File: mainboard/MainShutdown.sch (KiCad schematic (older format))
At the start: 21 parts, among them J10 AIR+, J6 AIR-, K1 KT12-1A, K2 G6DN 12V, Q1 NTR4003N, U13 TS3704IPT, U14 CD4044, U15 CD4082, U4 MainBoard_AD8244

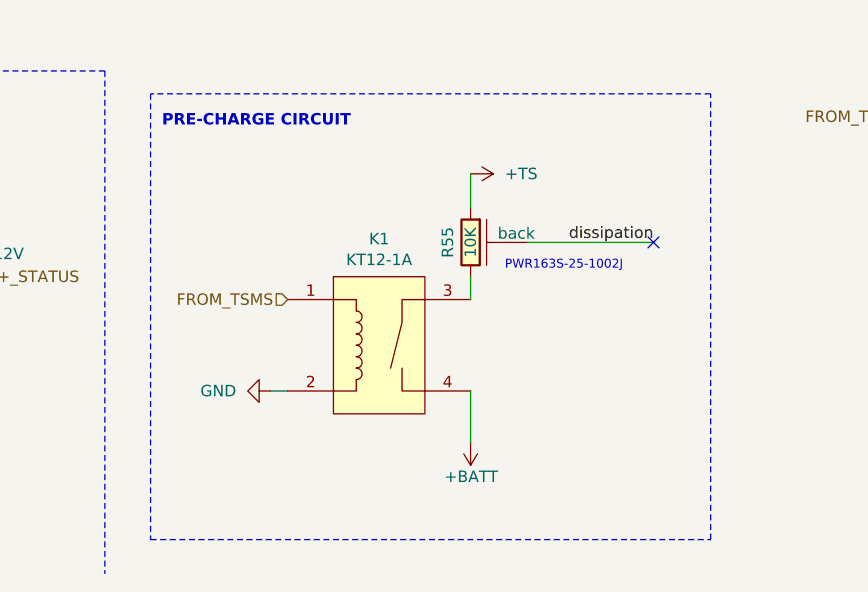
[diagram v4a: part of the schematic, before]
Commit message: added precharge rele suppression diode
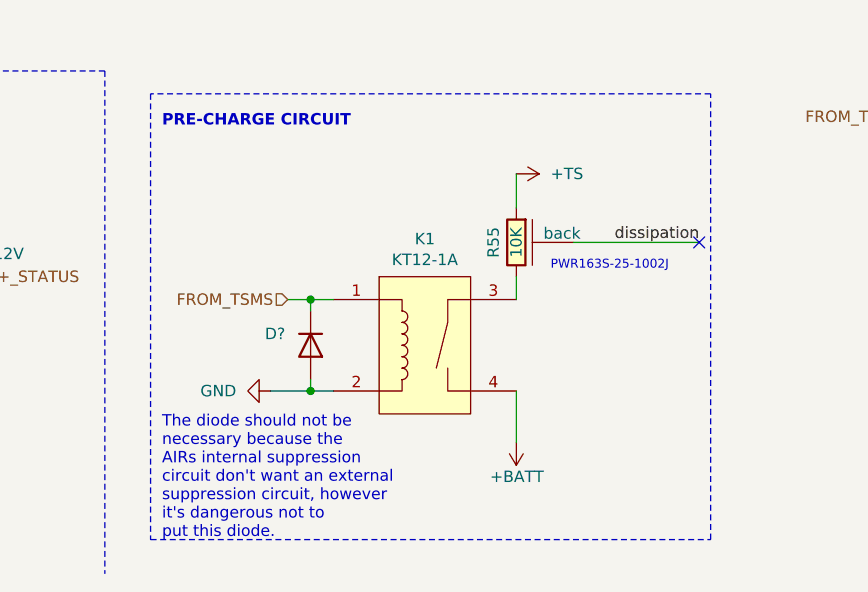
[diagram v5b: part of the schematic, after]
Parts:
- added D?: D, MainBoard:SOD_323HE, symbol Device:D
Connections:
- net FROM_TSMS: now also D?.1 (K)
- net GND: now also D?.2 (A)
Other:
- note added: "The diode should not be \nnecessary because the \nAIRs internal suppression \ncircuit don't want an external \nsuppression circuit, however \nit's dangerous not to \nput this diode."
- moved on the sheet: K1, R55
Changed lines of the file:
@@
 Comment4 ""
 $EndDescr
-Text Notes 6000 6375 0    39   ~ 0
+Text Notes 6200 6375 0    39   ~ 0
 PWR163S-25-1002J
 $Comp
 L MainBoard:+TS #PWR0148
 U 1 1 5B0DE0E2
-P 5850 5950
-F 0 "#PWR0148" H 5850 5800 50  0001 C CNN
-F 1 "+TS" V 5850 6100 50  0000 L CNN
-F 2 "" H 5750 5700 50  0001 C CNN
-F 3 "" H 5850 5800 50  0001 C CNN
-	1    5850 5950
+P 6050 5950
+F 0 "#PWR0148" H 6050 5800 50  0001 C CNN
+F 1 "+TS" V 6050 6100 50  0000 L CNN
+F 2 "" H 5950 5700 50  0001 C CNN
+F 3 "" H 6050 5800 50  0001 C CNN
+	1    6050 5950
 	0    1    1    0
 $EndComp
@@
 L power:+BATT #PWR0147
 U 1 1 5C2C487D
-P 5850 7125
-F 0 "#PWR0147" H 5850 6975 50  0001 C CNN
-F 1 "+BATT" H 5730 7275 50  0000 L CNN
-F 2 "" H 5850 7125 50  0001 C CNN
-F 3 "" H 5850 7125 50  0001 C CNN
-	1    5850 7125
+P 6050 7125
+F 0 "#PWR0147" H 6050 6975 50  0001 C CNN
+F 1 "+BATT" H 5930 7275 50  0000 L CNN
+F 2 "" H 6050 7125 50  0001 C CNN
+F 3 "" H 6050 7125 50  0001 C CNN
+	1    6050 7125
 	-1   0    0    1
 $EndComp
 Wire Wire Line
-	5850 6400 5850 6500
-Wire Wire Line
-	5850 6100 5850 5950
-Wire Wire Line
-	5850 6900 5850 7125
+	6050 6400 6050 6500
+Wire Wire Line
+	6050 6100 6050 5950
+Wire Wire Line
+	6050 6900 6050 7125
 $Comp
 L MainBoard:KT12-1A K1
 U 1 1 5E5A93F5
-P 5450 6700
-F 0 "K1" H 5450 7165 50  0000 C CNN
-F 1 "KT12-1A" H 5450 7074 50  0000 C CNN
-F 2 "MainBoard:KT_THT" H 5450 6350 50  0001 C CNN
-F 3 "https://standexelectronics.com/viewer/pdfjs/web/viewer.php?file=https%3A%2F%2Fstandexelectronics.com%2Fwp-content%2Fuploads%2F2015%2F03%2FKT_V03.pdf" H 5450 6700 50  0001 C CNN
-	1    5450 6700
+P 5650 6700
+F 0 "K1" H 5650 7165 50  0000 C CNN
+F 1 "KT12-1A" H 5650 7074 50  0000 C CNN
+F 2 "MainBoard:KT_THT" H 5650 6350 50  0001 C CNN
+F 3 "https://standexelectronics.com/viewer/pdfjs/web/viewer.php?file=https%3A%2F%2Fstandexelectronics.com%2Fwp-content%2Fuploads%2F2015%2F03%2FKT_V03.pdf" H 5650 6700 50  0001 C CNN
+	1    5650 6700
 	1    0    0    -1
 $EndComp
@@
 L MainBoard:R_power_backplane R55
 U 1 1 5DC7CE9F
-P 5850 6250
-F 0 "R55" V 5950 6250 50  0000 C CNN
-F 1 "10K" V 5850 6250 50  0000 C CNN
-F 2 "MainBoard:pwr163" V 5810 6250 50  0001 C CNN
-F 3 "~" H 5850 6250 50  0001 C CNN
-F 4 "https://www.mouser.it/ProductDetail/Bourns/PWR163S-25-1002J?qs=%2Fha2pyFadugfff1oC4vY%252Bes8I7FN4jgvWF%2FMj%252B7BM%2FJuTCfu5H9AeA%3D%3D" H 5850 6250 50  0001 C CNN "Mouser"
-	1    5850 6250
+P 6050 6250
+F 0 "R55" V 6150 6250 50  0000 C CNN
+F 1 "10K" V 6050 6250 50  0000 C CNN
+F 2 "MainBoard:pwr163" V 6010 6250 50  0001 C CNN
+F 3 "~" H 6050 6250 50  0001 C CNN
+F 4 "https://www.mouser.it/ProductDetail/Bourns/PWR163S-25-1002J?qs=%2Fha2pyFadugfff1oC4vY%252Bes8I7FN4jgvWF%2FMj%252B7BM%2FJuTCfu5H9AeA%3D%3D" H 6050 6250 50  0001 C CNN "Mouser"
+	1    6050 6250
 	-1   0    0    1
 $EndComp
@@
 Text HLabel 1600 6300 2    50   Input ~ 0
 AIR-_STATUS
-Text Label 6650 6250 2    50   ~ 0
+Text Label 6850 6250 2    50   ~ 0
 dissipation
 Wire Wire Line
-	6100 6250 6650 6250
-NoConn ~ 6650 6250
+	6300 6250 6850 6250
+NoConn ~ 6850 6250
 Text HLabel 2800 3050 0    50   Input ~ 0
 RESET_BUTTON
@@
 Text HLabel 5050 6500 0    50   Input ~ 0
 FROM_TSMS
-Wire Wire Line
-	4975 6900 5050 6900
 $Comp
 L power:GND #PWR0145
@@
 Wire Wire Line
 	3050 6300 3000 6300
+$Comp
+L Device:D D?
+U 1 1 60603EB1
+P 5150 6700
+AR Path="/60603EB1" Ref="D?"  Part="1"
+AR Path="/5B045B0D/60603EB1" Ref="D?"  Part="1"
+F 0 "D?" V 5100 6500 50  0000 L CNN
+F 1 "D" V 5200 6500 50  0001 L CNN
+F 2 "MainBoard:SOD_323HE" H 5150 6700 50  0001 C CNN
+F 3 "~" H 5150 6700 50  0001 C CNN
+	1    5150 6700
+	0    1    1    0
+$EndComp
+Wire Wire Line
+	4975 6900 5150 6900
+Wire Wire Line
+	5150 6850 5150 6900
+Connection ~ 5150 6900
+Wire Wire Line
+	5150 6900 5250 6900
+Wire Wire Line
+	5050 6500 5150 6500
+Wire Wire Line
+	5150 6500 5150 6550
+Wire Wire Line
+	5250 6500 5150 6500
+Connection ~ 5150 6500
+Text Notes 4500 7550 0    50   ~ 0
+The diode should not be \nnecessary because the \nAIRs internal suppression \ncircuit don't want an external \nsuppression circuit, however \nit's dangerous not to \nput this diode.
 $EndSCHEMATC

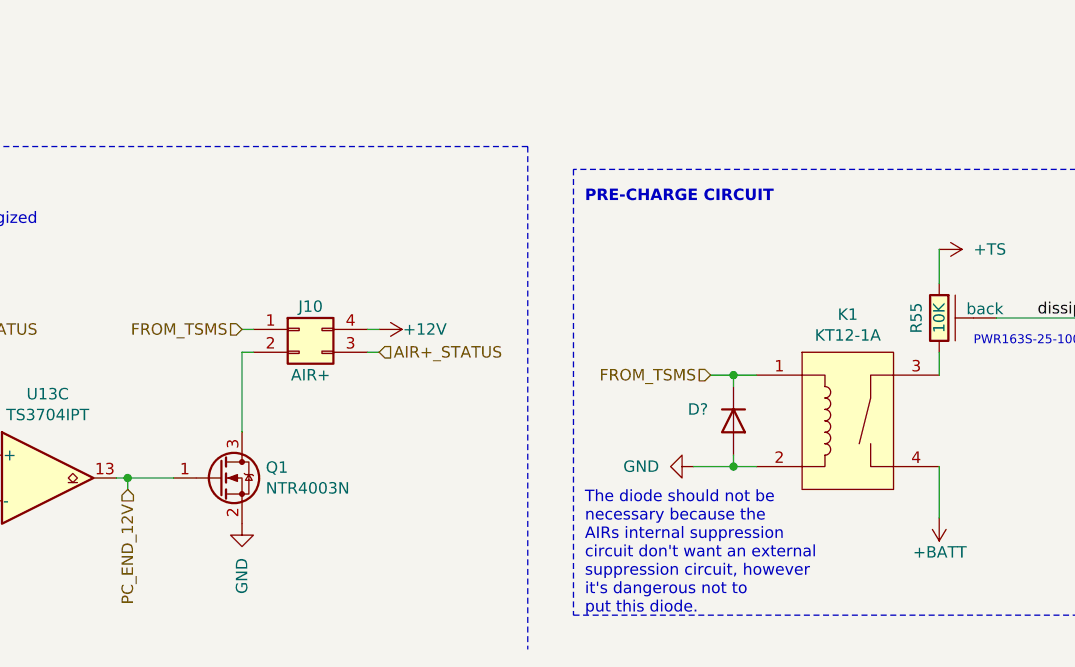
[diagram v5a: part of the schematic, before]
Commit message: commented AIR suppression
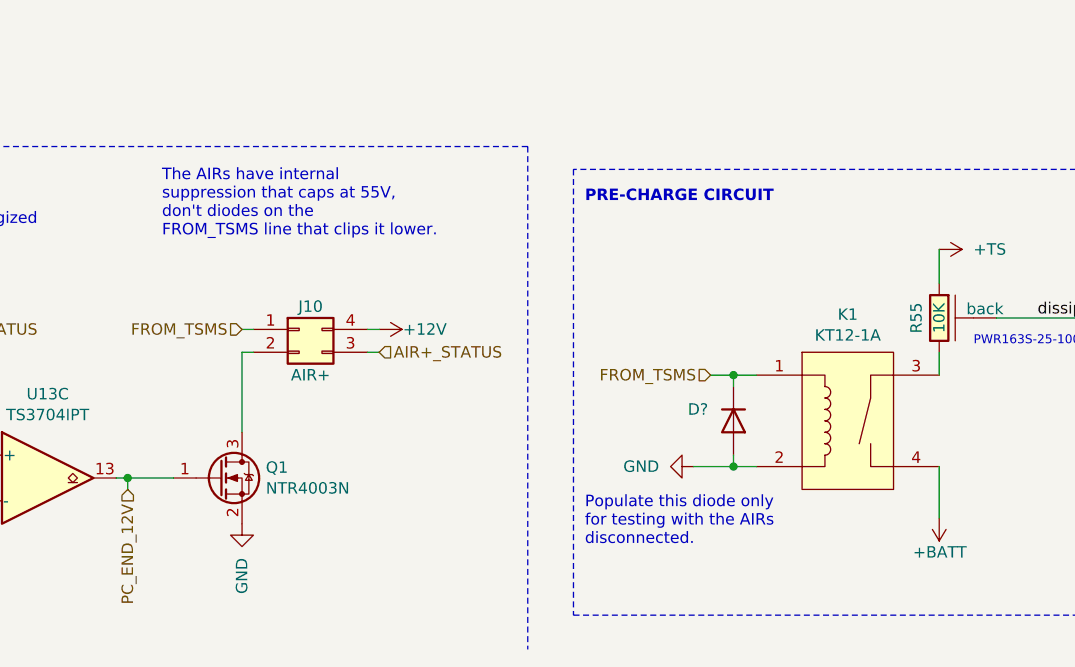
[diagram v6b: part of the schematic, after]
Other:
- note added: "Populate this diode only\nfor testing with the AIRs \ndisconnected."
- note added: "The AIRs have internal \nsuppression that caps at 55V, \ndon't diodes on the \nFROM_TSMS line that clips it lower."
- note removed: "The diode should not be \nnecessary because the \nAIRs internal suppression \ncircuit don't want an external \nsuppression circuit, however \nit's dangerous not to \nput this diode."
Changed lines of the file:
@@
 	5250 6500 5150 6500
 Connection ~ 5150 6500
-Text Notes 4500 7550 0    50   ~ 0
-The diode should not be \nnecessary because the \nAIRs internal suppression \ncircuit don't want an external \nsuppression circuit, however \nit's dangerous not to \nput this diode.
+Text Notes 4500 7250 0    50   ~ 0
+Populate this diode only\nfor testing with the AIRs \ndisconnected.
+Text Notes 2650 5900 0    50   ~ 0
+The AIRs have internal \nsuppression that caps at 55V, \ndon't diodes on the \nFROM_TSMS line that clips it lower.
 $EndSCHEMATC

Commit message: modifieed comment
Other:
- note added: "The AIRs have internal \nsuppression that caps at 55V, \ndon't put flyback diodes on the \nFROM_TSMS line that clips it lower."
- note removed: "The AIRs have internal \nsuppression that caps at 55V, \ndon't diodes on the \nFROM_TSMS line that clips it lower."
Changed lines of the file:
@@
 Populate this diode only\nfor testing with the AIRs \ndisconnected.
 Text Notes 2650 5900 0    50   ~ 0
-The AIRs have internal \nsuppression that caps at 55V, \ndon't diodes on the \nFROM_TSMS line that clips it lower.
+The AIRs have internal \nsuppression that caps at 55V, \ndon't put flyback diodes on the \nFROM_TSMS line that clips it lower.
 $EndSCHEMATC

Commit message: v1.1 as printed
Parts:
- removed D?: D, MainBoard:SOD_323HE, symbol Device:D
- removed J10: AIR+, MainBoard:Molex_Micro-Fit_3.0_43045-0412_2x02_P3.00mm_Vertical, symbol Connector_Generic:Conn_02x02_Counter_Clockwise
- removed J6: AIR-, MainBoard:Molex_Micro-Fit_3.0_43045-0412_2x02_P3.00mm_Vertical, symbol Connector_Generic:Conn_02x02_Counter_Clockwise
- removed K1: KT12-1A, MainBoard:KT_THT, symbol MainBoard:KT12-1A
- removed Q1, Q?: NTR4003N, Package_TO_SOT_SMD:SOT-23, symbol Device:Q_NMOS_GSD
- removed R55: 10K, MainBoard:pwr163, symbol MainBoard:R_power_backplane
- removed unit 3 of U13
- added JP7: SolderJumper_2_Open, Jumper:SolderJumper-2_P1.3mm_Open_RoundedPad1.0x1.5mm, symbol Jumper:SolderJumper_2_Open
- added Q2: DMN10H220L, Package_TO_SOT_SMD:SOT-23, symbol Transistor_FET:DMN10H220L
- added Q8, Q9: NTR5105PT1G, Package_TO_SOT_SMD:SOT-23, symbol Device:Q_PMOS_GSD
- added R39, R40: 0, Resistor_SMD:R_0603_1608Metric, symbol Device:R
- added RN21: 22, MainBoard:R_network_4x1_bourns_CAY16, symbol Device:R_Pack04_Split
- added SW2: SD_RESET, MainBoard:Button_SMD_6x3.5x4.3mm, symbol MainBoard:SW_Push
- added TP24: SD_OK, TestPoint:TestPoint_Pad_D1.0mm, symbol Connector:TestPoint
- added TP25: BMS_LATCHED, TestPoint:TestPoint_Pad_D1.0mm, symbol Connector:TestPoint
- added TP26: IMD_LATCHED, TestPoint:TestPoint_Pad_D1.0mm, symbol Connector:TestPoint
- added TP27: TS_ON, TestPoint:TestPoint_Pad_D1.0mm, symbol Connector:TestPoint
- added TP28: TS_ON_12V, TestPoint:TestPoint_Pad_D1.0mm, symbol Connector:TestPoint
- added unit 3 of U13
- D14: value 12V -> DDZ13ASF 13V
- U13: symbol Comparator:LM339 -> MainBoard:TS3704
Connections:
- net +12V: now also Q8.2 (S), Q9.2 (S)
- net BMS_LATCHED: now also R39.2, RN21.6 (R3.2), TP25.1
- net BMS_LED: now also Q8.3 (D)
- net EN_BMS_SD: now also R39.1
- net EN_IMD_SD: now also R40.1
- net GND: now also JP7.1 (A), Q2.2 (S), SW2.2
- net IMD_LATCHED: now also R40.2, RN21.5 (R4.2), TP26.1
- net IMD_LED: now also Q9.3 (D)
- net RESET_BUTTON: now also JP7.2 (B), SW2.1
- net SD_OK: now also RN21.2 (R2.1), TP24.1
- net TS_ON: now also TP27.1
- net TS_ON_12V: now also TP28.1
- net VREF_1.5V: now also U13.10 (-)
- net at D15.2 (A), K2.1: now also Q2.3 (D)
- new net: Q2.1 (G), RN21.7 (R2.2)
- new net: Q9.1 (G), RN21.4 (R4.1)
- new net: Q8.1 (G), RN21.3 (R3.1)
- no-connect marks 9 -> 10
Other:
- note added: "Buffering signals, CD4044 can't \nsource/sink more than 1mA.\nCan be not placed if jumpers are in place"
- note added: "DNP"
- note added: "RESET BUTTON WITH PULLUP (100K) FOR AMS AND IMD FAULT \nWITH START DELAY OF 120ms \n(BECAUSE OF C=1uF AND\nVIH MIN OF 4044 is 8.4V AT VCC=12V)"
- note added: "TODO: ASK_LED WIRING\n"
- note removed: "AIR CONTROL CIRCUIT\n"
- note removed: "AIR connector:\nPIN 1,2: Main coil\nPIN 3,4: NO contact, closed when energized"
- note removed: "Buffering signals, CD4044 can't \nsource/sink more than 1mA"
- note removed: "PRE-CHARGE CIRCUIT"
- note removed: "PWR163S-25-1002J"
- note removed: "Populate this diode only\nfor testing with the AIRs \ndisconnected."
- note removed: "RESET BUTTON WITH PULLUP (100K) FOR AMS AND IMD FAULT \nWITH START DELAY OF 120ms (BECAUSE OF C=1uF AND\nVIH MIN OF 4044 is 8.4V AT VCC=12V)"
- note removed: "The AIRs have internal \nsuppression that caps at 55V, \ndon't put flyback diodes on the \nFROM_TSMS line that clips it lower."
- moved on the sheet: C33, C34, C35, C47, D15, K2, R54, R9, RN13, U15B
